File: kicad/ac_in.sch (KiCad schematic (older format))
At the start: 28 parts, among them J701 tblock, U702 R-78B3.3-2.0, U704 R-78E5.0-1.0, U706 AP2114H-1.2TRG1

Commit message: moving ethernet connector to right and depopulate 15vh
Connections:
- no-connect marks 0 -> 1
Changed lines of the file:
@@
 Wire Wire Line
 	6350 6450 6000 6450
+NoConn ~ 12550 5550
 $EndSCHEMATC

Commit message: roouting and more routing.... I think 4 layers WONT be enought
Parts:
- removed C702: 220uF, servo:C_0603_1608Metric, symbol servo:Capacitor
- removed U704: R-78E5.0-1.0, Converter_DCDC:Converter_DCDC_RECOM_R-78E-0.5_THT, symbol servo:R-78E5.0-1.0
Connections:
- net labels added: 5VH_IN
- net labels removed: 15VH, 15VH_IN
- wire segments 112 -> 103
- no-connect marks 1 -> 0
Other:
- moved on the sheet: C708, C710, D704, R704
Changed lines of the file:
@@
 $EndComp
-$Comp
-L servo:Capacitor C?
-U 1 1 5E2F90CF
-P 14300 6050
-AR Path="/5EAA846A/5E2F90CF" Ref="C?"  Part="1"
-AR Path="/5DD76B18/5E2F90CF" Ref="C708"  Part="1"
-F 0 "C708" V 14328 6160 20  0000 L CNN
-F 1 "22uF" V 14371 6160 20  0000 L CNN
-F 2 "servo:C_0603_1608Metric" H 14300 5950 60  0001 C CNN
-F 3 "" H 14300 6050 60  0000 C CNN
-F 4 "22uF" V 1300 6450 60  0001 C CNN "ValueDisplayed"
-	1    14300 6050
-	0    1    1    0
-$EndComp
-$Comp
-L servo:Capacitor C?
-U 1 1 5E18DDC4
-P 14600 6050
-AR Path="/5EAA846A/5E18DDC4" Ref="C?"  Part="1"
-AR Path="/5DD76B18/5E18DDC4" Ref="C710"  Part="1"
-F 0 "C710" V 14628 6160 20  0000 L CNN
-F 1 "100nF" V 14671 6160 20  0000 L CNN
-F 2 "servo:C_0603_1608Metric" H 14600 5950 60  0001 C CNN
-F 3 "" H 14600 6050 60  0000 C CNN
-F 4 "22uF" V 1600 6450 60  0001 C CNN "ValueDisplayed"
-	1    14600 6050
-	0    1    1    0
-$EndComp
-Wire Wire Line
-	13850 6050 13850 6550
-Wire Wire Line
-	13350 5650 13350 5750
-$Comp
-L servo:15VH #PWR0710
-U 1 1 5E18DDC5
-P 13350 5650
-F 0 "#PWR0710" H 13350 5450 20  0001 C CNN
-F 1 "15VH" H 13355 5807 28  0000 C CNN
-F 2 "" H 13350 5650 50  0001 C CNN
-F 3 "" H 13350 5650 50  0001 C CNN
-	1    13350 5650
-	1    0    0    -1
-$EndComp
-Wire Wire Line
-	13350 5750 13550 5750
 $Comp
 L servo:5VH #PWR0717
 U 1 1 5E309ABD
-P 15000 5650
-F 0 "#PWR0717" H 15000 5450 20  0001 C CNN
-F 1 "5VH" H 15005 5807 28  0000 C CNN
-F 2 "" H 15000 5650 50  0001 C CNN
-F 3 "" H 15000 5650 50  0001 C CNN
-	1    15000 5650
-	1    0    0    -1
-$EndComp
-Wire Wire Line
-	13850 6550 14000 6550
+P 13650 5450
+F 0 "#PWR0717" H 13650 5250 20  0001 C CNN
+F 1 "5VH" H 13655 5607 28  0000 C CNN
+F 2 "" H 13650 5450 50  0001 C CNN
+F 3 "" H 13650 5450 50  0001 C CNN
+	1    13650 5450
+	1    0    0    -1
+$EndComp
 $Comp
 L servo:Resistor R?
 U 1 1 5E38D647
-P 15000 6000
+P 13650 5800
 AR Path="/5EAA846A/5E38D647" Ref="R?"  Part="1"
 AR Path="/5DD76B18/5E38D647" Ref="R704"  Part="1"
-F 0 "R704" V 14978 6050 20  0000 L CNN
-F 1 "680" V 15021 6050 20  0000 L CNN
-F 2 "Resistor_SMD:R_0603_1608Metric" H 14500 5900 60  0001 C CNN
-F 3 "" H 14600 6000 60  0001 C CNN
-F 4 "680" V 2600 6400 60  0001 C CNN "ValueDisplayed"
-	1    15000 6000
+F 0 "R704" V 13628 5850 20  0000 L CNN
+F 1 "680" V 13671 5850 20  0000 L CNN
+F 2 "Resistor_SMD:R_0603_1608Metric" H 13150 5700 60  0001 C CNN
+F 3 "" H 13250 5800 60  0001 C CNN
+F 4 "680" V 1250 6200 60  0001 C CNN "ValueDisplayed"
+	1    13650 5800
 	0    1    1    0
 $EndComp
@@
 L servo:LED_A2_K1 D?
 U 1 1 5E38D64F
-P 15000 6300
+P 13650 6100
 AR Path="/5EAA846A/5E38D64F" Ref="D?"  Part="1"
 AR Path="/5DD76B18/5E38D64F" Ref="D704"  Part="1"
-F 0 "D704" V 15025 6430 20  0000 L CNN
-F 1 "red" H 15000 6450 16  0001 C CNN
-F 2 "servo:LED_0603_1608Metric" H 14800 6100 60  0001 C CNN
-F 3 "" H 14800 6100 60  0000 C CNN
-F 4 "red" V 2600 6200 60  0001 C CNN "VALUE"
-	1    15000 6300
-	0    1    1    0
-$EndComp
-Wire Wire Line
-	15000 6450 15000 6550
-Wire Wire Line
-	15000 5800 15000 5750
+F 0 "D704" V 13675 6230 20  0000 L CNN
+F 1 "red" H 13650 6250 16  0001 C CNN
+F 2 "servo:LED_0603_1608Metric" H 13450 5900 60  0001 C CNN
+F 3 "" H 13450 5900 60  0000 C CNN
+F 4 "red" V 1250 6000 60  0001 C CNN "VALUE"
+	1    13650 6100
+	0    1    1    0
+$EndComp
+Wire Wire Line
+	13650 6250 13650 6350
 $Comp
 L servo:GND #PWR?
@@
 $EndComp
 $Comp
-L servo:15VH #PWR0704
-U 1 1 5E18DDCC
-P 12800 5450
-F 0 "#PWR0704" H 12800 5250 20  0001 C CNN
-F 1 "15VH" H 12853 5494 28  0000 L CNN
-F 2 "" H 12800 5450 50  0001 C CNN
-F 3 "" H 12800 5450 50  0001 C CNN
-	1    12800 5450
-	1    0    0    -1
-$EndComp
-$Comp
 L servo:GNDH #PWR0702
 U 1 1 5E18DDCD
-P 12300 6350
-F 0 "#PWR0702" H 12300 6100 30  0001 C CNN
-F 1 "GNDH" H 12300 6192 30  0000 C CNN
-F 2 "" H 12300 6350 50  0001 C CNN
-F 3 "" H 12300 6350 50  0001 C CNN
-	1    12300 6350
-	1    0    0    -1
-$EndComp
-$Comp
-L servo:Capacitor C?
-U 1 1 5E18DDCF
-P 13350 6050
-AR Path="/5EAA846A/5E18DDCF" Ref="C?"  Part="1"
-AR Path="/5DD76B18/5E18DDCF" Ref="C702"  Part="1"
-F 0 "C702" V 13378 5941 20  0000 R CNN
-F 1 "220uF" V 13421 5941 20  0000 R CNN
-F 2 "servo:C_0603_1608Metric" H 13350 5950 60  0001 C CNN
-F 3 "" H 13350 6050 60  0000 C CNN
-F 4 "22uF" V 350 6450 60  0001 C CNN "ValueDisplayed"
-	1    13350 6050
-	0    1    1    0
-$EndComp
-Wire Wire Line
-	13350 5750 13350 5950
-Connection ~ 13350 5750
-Wire Wire Line
-	13850 6550 13350 6550
-Connection ~ 13850 6550
+P 12300 6400
+F 0 "#PWR0702" H 12300 6150 30  0001 C CNN
+F 1 "GNDH" H 12300 6242 30  0000 C CNN
+F 2 "" H 12300 6400 50  0001 C CNN
+F 3 "" H 12300 6400 50  0001 C CNN
+	1    12300 6400
+	1    0    0    -1
+$EndComp
 Text Notes 5550 4700 0    197  ~ 39
 COLD SUPPLY\n
@@
 	6850 6050 6850 6450
 Connection ~ 6850 6450
-Connection ~ 15000 5750
-Wire Wire Line
-	15000 5650 15000 5750
 Connection ~ 2000 5900
 Wire Wire Line
@@
 Text Notes 13500 5100 0    20   ~ 0
 Take in account that hot doesn't mean that it is refered to high voltage\n AC socket input path like 220v/380v. It is intended to isolate the uC\n/logic/user interfase side from accidentally high voltage contact on the\n hot side and prevent injuries as to make the reinforced isolation\n possible with one single isolateion added
-Text Notes 13650 5500 0    20   ~ 0
-sip 3 package, cheap, easy to \nreplace and many options
 Text Notes 5000 5400 0    20   ~ 0
 sip 3 package, cheap, easy to \nreplace and many options
@@
 Text Notes 6050 4950 0    20   ~ 0
 It is inteded to use only, I mean ONLY inside the control board, none of\n these coopers wires has to leave the board. I isolate every single pin\n from these supply to go outside, take these in account\n
-$Comp
-L servo:GNDH #PWR0713
-U 1 1 5EC79A03
-P 14000 6600
-F 0 "#PWR0713" H 14000 6350 30  0001 C CNN
-F 1 "GNDH" H 14000 6442 30  0000 C CNN
-F 2 "" H 14000 6600 50  0001 C CNN
-F 3 "" H 14000 6600 50  0001 C CNN
-	1    14000 6600
-	1    0    0    -1
-$EndComp
-Wire Wire Line
-	14000 6600 14000 6550
-Connection ~ 14000 6550
 Wire Wire Line
 	2000 5750 2000 5900
@@
 Text Notes 6400 6250 0    20   ~ 0
 the intention of the LCD it to clean \nthe noise without using big filters\n and L's. It's recommended and \ntested that these method works \npretty\nlow noise \nLDO <30uV
-$Comp
-L servo:R-78E5.0-1.0 U704
-U 1 1 5E2CE6E1
-P 13850 5750
-F 0 "U704" H 13850 5968 39  0000 C CNN
-F 1 "R-78E5.0-1.0" H 13850 5893 39  0000 C CNN
-F 2 "Converter_DCDC:Converter_DCDC_RECOM_R-78E-0.5_THT" H 13900 5500 50  0001 L CIN
-F 3 "https://www.recom-power.com/pdf/Innoline/R-78Exx-1.0.pdf" H 13850 5750 50  0001 C CNN
-	1    13850 5750
-	1    0    0    -1
-$EndComp
-Wire Wire Line
-	14150 5750 14300 5750
-Wire Wire Line
-	14000 6550 14300 6550
-Wire Wire Line
-	13350 6250 13350 6550
-Wire Wire Line
-	14300 5950 14300 5750
-Connection ~ 14300 5750
-Wire Wire Line
-	14300 5750 14600 5750
-Wire Wire Line
-	14600 5950 14600 5750
-Connection ~ 14600 5750
-Wire Wire Line
-	14600 5750 15000 5750
-Wire Wire Line
-	14300 6250 14300 6550
-Connection ~ 14300 6550
-Wire Wire Line
-	14300 6550 14600 6550
-Wire Wire Line
-	14600 6250 14600 6550
-Connection ~ 14600 6550
-Wire Wire Line
-	14600 6550 15000 6550
 $Comp
 L servo:PWR_FLAG #FLG0701
@@
 $EndComp
 Wire Wire Line
-	12300 6250 12300 6300
-Wire Wire Line
-	12100 6300 12100 6050
+	12300 6250 12300 6350
+Wire Wire Line
+	12100 6350 12100 6050
 Wire Wire Line
 	12100 5850 12100 5550
@@
 	12650 5550 12700 5550
 Wire Wire Line
-	12800 5450 12800 5550
-Wire Wire Line
 	12300 5550 12450 5550
 Wire Wire Line
-	12300 6350 12300 6300
-Connection ~ 12300 6300
-Wire Wire Line
-	12100 6300 12300 6300
+	12300 6400 12300 6350
+Connection ~ 12300 6350
+Wire Wire Line
+	12100 6350 12300 6350
 Wire Wire Line
 	3550 6350 3550 6400
@@
 $EndComp
 Connection ~ 12700 5550
-Wire Wire Line
-	12700 5550 12800 5550
 $Comp
 L servo:PWR_FLAG #FLG0704
@@
 AC_N
 Text Label 12150 5550 0    20   ~ 0
-15VH_IN
+5VH_IN
 Text Label 3150 5900 0    20   ~ 0
 5VC_IN
@@
 Wire Wire Line
 	6350 6450 6000 6450
-NoConn ~ 12550 5550
+Wire Wire Line
+	13250 6350 13650 6350
+Connection ~ 13250 6350
+Wire Wire Line
+	13250 6050 13250 6350
+Wire Wire Line
+	12950 6350 13250 6350
+Wire Wire Line
+	13650 5450 13650 5550
+Wire Wire Line
+	13650 5600 13650 5550
+Connection ~ 13650 5550
+Wire Wire Line
+	13250 5550 13650 5550
+Wire Wire Line
+	13250 5750 13250 5550
+Connection ~ 13250 5550
+Wire Wire Line
+	12950 5550 13250 5550
+Wire Wire Line
+	12950 5750 12950 5550
+Connection ~ 12950 5550
+$Comp
+L servo:Capacitor C?
+U 1 1 5E18DDC4
+P 13250 5850
+AR Path="/5EAA846A/5E18DDC4" Ref="C?"  Part="1"
+AR Path="/5DD76B18/5E18DDC4" Ref="C710"  Part="1"
+F 0 "C710" V 13278 5960 20  0000 L CNN
+F 1 "100nF" V 13321 5960 20  0000 L CNN
+F 2 "servo:C_0603_1608Metric" H 13250 5750 60  0001 C CNN
+F 3 "" H 13250 5850 60  0000 C CNN
+F 4 "22uF" V 250 6250 60  0001 C CNN "ValueDisplayed"
+	1    13250 5850
+	0    1    1    0
+$EndComp
+$Comp
+L servo:Capacitor C?
+U 1 1 5E2F90CF
+P 12950 5850
+AR Path="/5EAA846A/5E2F90CF" Ref="C?"  Part="1"
+AR Path="/5DD76B18/5E2F90CF" Ref="C708"  Part="1"
+F 0 "C708" V 12978 5960 20  0000 L CNN
+F 1 "22uF" V 13021 5960 20  0000 L CNN
+F 2 "servo:C_0603_1608Metric" H 12950 5750 60  0001 C CNN
+F 3 "" H 12950 5850 60  0000 C CNN
+F 4 "22uF" V -50 6250 60  0001 C CNN "ValueDisplayed"
+	1    12950 5850
+	0    1    1    0
+$EndComp
+Wire Wire Line
+	12700 5550 12950 5550
+Wire Wire Line
+	12300 6350 12950 6350
+Connection ~ 12950 6350
+Wire Wire Line
+	12950 6300 12950 6350
+Wire Wire Line
+	12950 6050 12950 6350
 $EndSCHEMATC

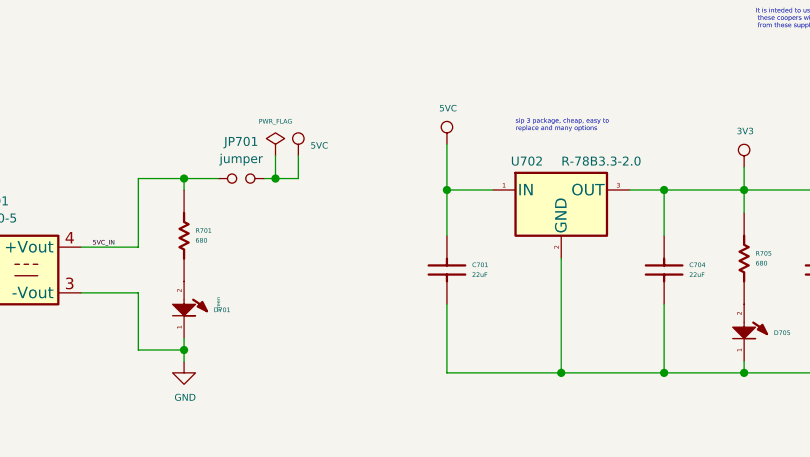
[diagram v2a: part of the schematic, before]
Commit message: ROUTING DONE!!!!!!!!!!!!!!!!!!!!!!!!!
ok, but....I need to improve all the nets, get them wider and so, but at
least all nets were routed to the uController.. it was more difucult
than I ever imagine... it tooks me 1 week only the uC coarse layout..
very very complex.. a lot of traces.. and with NO blind vias.. so it'll
be cheaper and any prototype manufacturer could do the board, and it'll
be more reliable..AND I'd test all nets on the board it it has at least
one via, or rout alongside top or bottom, so it's all the nets.. for
debug, it's very important...
lets do some improvement...
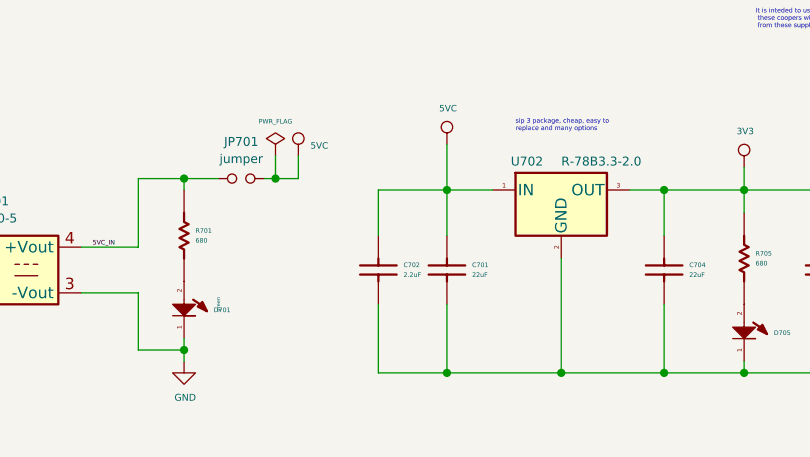
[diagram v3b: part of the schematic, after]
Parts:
- added C702: 2.2uF, servo:C_0603_1608Metric, symbol servo:Capacitor
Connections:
- wire segments 103 -> 107
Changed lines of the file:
@@
-$EndComp
-$Comp
-L servo:Capacitor C?
-U 1 1 5E286219
-P 7750 5950
-AR Path="/5EAA846A/5E286219" Ref="C?"  Part="1"
-AR Path="/5DD76B18/5E286219" Ref="C714"  Part="1"
-F 0 "C714" V 7778 6060 20  0000 L CNN
-F 1 "100nF" V 7821 6060 20  0000 L CNN
-F 2 "servo:C_0603_1608Metric" H 7750 5850 60  0001 C CNN
-F 3 "" H 7750 5950 60  0000 C CNN
-F 4 "22uF" V -5250 6350 60  0001 C CNN "ValueDisplayed"
-	1    7750 5950
-	0    1    1    0
 $EndComp
 $Comp
@@
 Connection ~ 7400 6450
 Wire Wire Line
-	7400 6450 7750 6450
-Wire Wire Line
-	7750 6150 7750 6450
-Connection ~ 7750 6450
-Wire Wire Line
-	7750 6450 8100 6450
-Wire Wire Line
 	7400 5850 7400 5650
 Connection ~ 7400 5650
-Wire Wire Line
-	7750 5850 7750 5650
-Wire Wire Line
-	7400 5650 7750 5650
-Connection ~ 7750 5650
-Wire Wire Line
-	7750 5650 8100 5650
 Text Notes 6400 6250 0    20   ~ 0
 the intention of the LCD it to clean \nthe noise without using big filters\n and L's. It's recommended and \ntested that these method works \npretty\nlow noise \nLDO <30uV
@@
 Wire Wire Line
 	12950 6050 12950 6350
+Wire Wire Line
+	7750 5650 8100 5650
+Wire Wire Line
+	7400 5650 7750 5650
+Connection ~ 7750 5650
+Wire Wire Line
+	7750 5850 7750 5650
+Wire Wire Line
+	7750 6450 8100 6450
+Wire Wire Line
+	7400 6450 7750 6450
+Connection ~ 7750 6450
+Wire Wire Line
+	7750 6150 7750 6450
+$Comp
+L servo:Capacitor C?
+U 1 1 5E286219
+P 7750 5950
+AR Path="/5EAA846A/5E286219" Ref="C?"  Part="1"
+AR Path="/5DD76B18/5E286219" Ref="C714"  Part="1"
+F 0 "C714" V 7778 6060 20  0000 L CNN
+F 1 "100nF" V 7821 6060 20  0000 L CNN
+F 2 "servo:C_0603_1608Metric" H 7750 5850 60  0001 C CNN
+F 3 "" H 7750 5950 60  0000 C CNN
+F 4 "22uF" V -5250 6350 60  0001 C CNN "ValueDisplayed"
+	1    7750 5950
+	0    1    1    0
+$EndComp
+$Comp
+L servo:Capacitor C?
+U 1 1 5E4CBAA0
+P 4400 5950
+AR Path="/5EAA846A/5E4CBAA0" Ref="C?"  Part="1"
+AR Path="/5DD76B18/5E4CBAA0" Ref="C702"  Part="1"
+F 0 "C702" V 4428 6060 20  0000 L CNN
+F 1 "2.2uF" V 4471 6060 20  0000 L CNN
+F 2 "servo:C_0603_1608Metric" H 4400 5850 60  0001 C CNN
+F 3 "" H 4400 5950 60  0000 C CNN
+F 4 "2.2uF" V -8100 1750 60  0001 C CNN "ValueDisplayed"
+	1    4400 5950
+	0    1    1    0
+$EndComp
+Wire Wire Line
+	4400 5850 4400 5650
+Wire Wire Line
+	4400 5650 4700 5650
+Wire Wire Line
+	4700 6450 4400 6450
+Wire Wire Line
+	4400 6450 4400 6150
+Connection ~ 4700 6450
 $EndSCHEMATC

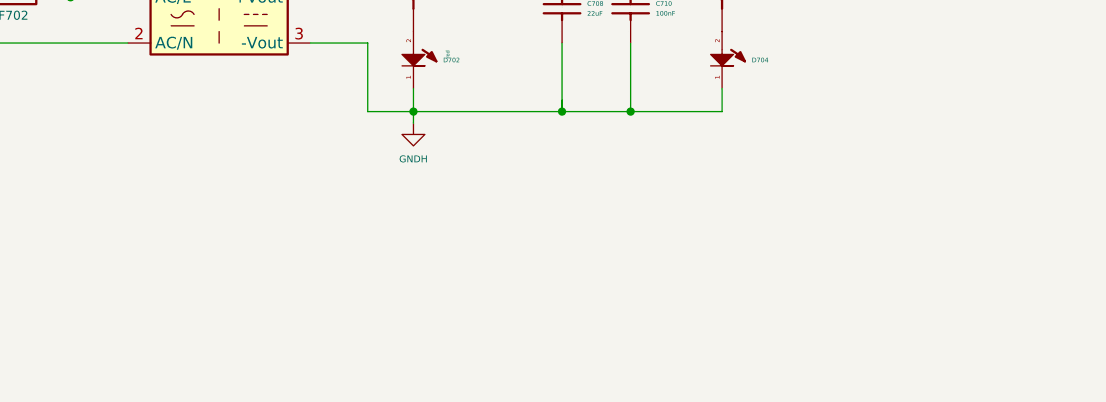
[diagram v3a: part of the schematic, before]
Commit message: change in 5v interface scenario.. remove bridges
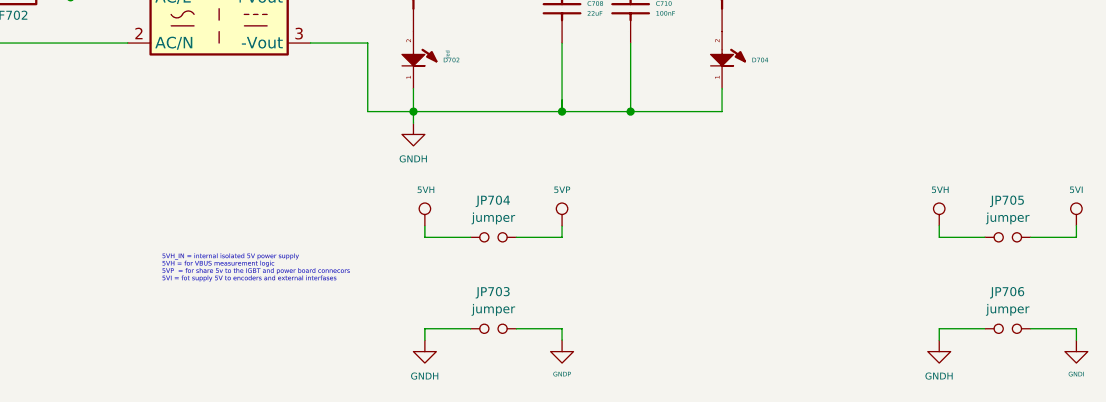
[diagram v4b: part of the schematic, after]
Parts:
- added JP703: jumper, servo:wire_bridge_38mm, symbol servo:jumper
- added JP704: jumper, servo:wire_bridge_44mm, symbol servo:jumper
- added JP705: jumper, servo:wire_bridge_50mm, symbol servo:jumper
- added JP706: jumper, servo:wire_bridge_60mm, symbol servo:jumper
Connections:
- net labels added: 5VI, 5VP, GNDI, GNDP
- wire segments 107 -> 123
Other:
- note added: "5VH_IN = internal isolated 5V power supply\n5VH = for VBUS measurement logic\n5VP = for share 5v to the IGBT and power board connecors\n5VI = fot supply 5V to encoders and external interfases\n"
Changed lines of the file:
@@
 $Descr A3 16535 11693
 encoding utf-8
-Sheet 7 19
+Sheet 7 20
 Title "AC input"
 Date "2020-01-09"
@@
 	4400 6450 4400 6150
 Connection ~ 4700 6450
+$Comp
+L servo:GNDH #PWR0254
+U 1 1 5ECD4F86
+P 12350 7350
+F 0 "#PWR0254" H 12350 7100 30  0001 C CNN
+F 1 "GNDH" H 12350 7192 30  0000 C CNN
+F 2 "" H 12350 7350 50  0001 C CNN
+F 3 "" H 12350 7350 50  0001 C CNN
+	1    12350 7350
+	1    0    0    -1
+$EndComp
+$Comp
+L servo:GNDP #PWR0255
+U 1 1 5ECD5091
+P 12950 7350
+F 0 "#PWR0255" H 12950 7100 30  0001 C CNN
+F 1 "GNDP" H 12950 7201 20  0000 C CNN
+F 2 "" H 12950 7350 50  0001 C CNN
+F 3 "" H 12950 7350 50  0001 C CNN
+	1    12950 7350
+	1    0    0    -1
+$EndComp
+$Comp
+L servo:5VP #PWR0256
+U 1 1 5ECD5194
+P 12950 6850
+F 0 "#PWR0256" H 12950 6650 20  0001 C CNN
+F 1 "5VP" H 12950 7007 28  0000 C CNN
+F 2 "" H 12950 6850 50  0001 C CNN
+F 3 "" H 12950 6850 50  0001 C CNN
+	1    12950 6850
+	1    0    0    -1
+$EndComp
+$Comp
+L servo:5VH #PWR0257
+U 1 1 5ECD533B
+P 12350 6850
+F 0 "#PWR0257" H 12350 6650 20  0001 C CNN
+F 1 "5VH" H 12355 7007 28  0000 C CNN
+F 2 "" H 12350 6850 50  0001 C CNN
+F 3 "" H 12350 6850 50  0001 C CNN
+	1    12350 6850
+	1    0    0    -1
+$EndComp
+$Comp
+L servo:jumper JP703
+U 1 1 5ECD557D
+P 12650 7300
+F 0 "JP703" H 12650 7461 39  0000 C CNN
+F 1 "jumper" H 12650 7386 39  0000 C CNN
+F 2 "servo:wire_bridge_38mm" H 12550 7280 50  0001 C CNN
+F 3 "~" H 12650 7380 50  0001 C CNN
+	1    12650 7300
+	1    0    0    -1
+$EndComp
+Wire Wire Line
+	12750 7300 12950 7300
+Wire Wire Line
+	12950 7300 12950 7350
+Wire Wire Line
+	12550 7300 12350 7300
+Wire Wire Line
+	12350 7300 12350 7350
+Wire Wire Line
+	12550 6900 12350 6900
+Wire Wire Line
+	12350 6900 12350 6850
+Wire Wire Line
+	12750 6900 12950 6900
+Wire Wire Line
+	12950 6900 12950 6850
+Text Notes 11200 7100 0    20   ~ 0
+5VH_IN = internal isolated 5V power supply\n5VH = for VBUS measurement logic\n5VP  = for share 5v to the IGBT and power board connecors\n5VI = fot supply 5V to encoders and external interfases\n
+$Comp
+L servo:GNDH #PWR0270
+U 1 1 5ECEC7F4
+P 14600 7350
+F 0 "#PWR0270" H 14600 7100 30  0001 C CNN
+F 1 "GNDH" H 14600 7192 30  0000 C CNN
+F 2 "" H 14600 7350 50  0001 C CNN
+F 3 "" H 14600 7350 50  0001 C CNN
+	1    14600 7350
+	1    0    0    -1
+$EndComp
+$Comp
+L servo:5VH #PWR0271
+U 1 1 5ECEC806
+P 14600 6850
+F 0 "#PWR0271" H 14600 6650 20  0001 C CNN
+F 1 "5VH" H 14605 7007 28  0000 C CNN
+F 2 "" H 14600 6850 50  0001 C CNN
+F 3 "" H 14600 6850 50  0001 C CNN
+	1    14600 6850
+	1    0    0    -1
+$EndComp
+Wire Wire Line
+	15000 7300 15200 7300
+Wire Wire Line
+	15200 7300 15200 7350
+Wire Wire Line
+	14800 7300 14600 7300
+Wire Wire Line
+	14600 7300 14600 7350
+Wire Wire Line
+	14800 6900 14600 6900
+Wire Wire Line
+	14600 6900 14600 6850
+Wire Wire Line
+	15000 6900 15200 6900
+Wire Wire Line
+	15200 6900 15200 6850
+$Comp
+L servo:GNDI #PWR0272
+U 1 1 5ECFE9BB
+P 15200 7350
+F 0 "#PWR0272" H 15200 7100 30  0001 C CNN
+F 1 "GNDI" H 15200 7201 20  0000 C CNN
+F 2 "" H 15200 7350 50  0001 C CNN
+F 3 "" H 15200 7350 50  0001 C CNN
+	1    15200 7350
+	1    0    0    -1
+$EndComp
+$Comp
+L servo:5VI #PWR0273
+U 1 1 5ECFEA79
+P 15200 6850
+F 0 "#PWR0273" H 15200 6650 20  0001 C CNN
+F 1 "5VI" H 15200 7007 28  0000 C CNN
+F 2 "" H 15200 6850 50  0001 C CNN
+F 3 "" H 15200 6850 50  0001 C CNN
+	1    15200 6850
+	1    0    0    -1
+$EndComp
+$Comp
+L servo:jumper JP704
+U 1 1 5E38023B
+P 12650 6900
+F 0 "JP704" H 12650 7061 39  0000 C CNN
+F 1 "jumper" H 12650 6986 39  0000 C CNN
+F 2 "servo:wire_bridge_44mm" H 12550 6880 50  0001 C CNN
+F 3 "~" H 12650 6980 50  0001 C CNN
+	1    12650 6900
+	1    0    0    -1
+$EndComp
+$Comp
+L servo:jumper JP705
+U 1 1 5E380332
+P 14900 6900
+F 0 "JP705" H 14900 7061 39  0000 C CNN
+F 1 "jumper" H 14900 6986 39  0000 C CNN
+F 2 "servo:wire_bridge_50mm" H 14800 6880 50  0001 C CNN
+F 3 "~" H 14900 6980 50  0001 C CNN
+	1    14900 6900
+	1    0    0    -1
+$EndComp
+$Comp
+L servo:jumper JP706
+U 1 1 5E38619B
+P 14900 7300
+F 0 "JP706" H 14900 7461 39  0000 C CNN
+F 1 "jumper" H 14900 7386 39  0000 C CNN
+F 2 "servo:wire_bridge_60mm" H 14800 7280 50  0001 C CNN
+F 3 "~" H 14900 7380 50  0001 C CNN
+	1    14900 7300
+	1    0    0    -1
+$EndComp
 $EndSCHEMATC
